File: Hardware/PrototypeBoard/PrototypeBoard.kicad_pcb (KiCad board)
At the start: 2 copper layers, 135 parts, among them J1 Motor, J2 Encoder, J3 ControlSupplyConnector, Q1 Q_NMOS_SGD, Q2 Q_NMOS_SGD, Q3 Q_NMOS_SGD, Q4 Q_NMOS_SGD, Q5 Q_NMOS_SGD, Q6 Q_NMOS_SGD, U1 TLI4970-D025T4, U2 TLI4970-D025T4, U3 TLI4970-D025T4, U4 TLE7185-1E, U5 ADC124S021

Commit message: some more layout work
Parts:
- moved TP31 227.2 mm to (262.9, 138.4)
- moved TP32 220.9 mm to (262.9, 143.5)
- moved TP33 209.2 mm to (260.4, 135.9)
- moved TP34 203.0 mm to (260.4, 141.0)
- moved TP3 194.6 mm to (234.9, 106.7)
- moved TP4 192.0 mm to (234.9, 116.8)
- moved TP5 190.1 mm to (234.9, 127.0)
- moved TP1 183.3 mm to (174.0, 156.2)
- moved TP21 177.9 mm to (209.6, 127.0)
- moved TP2 172.5 mm to (174.0, 148.6)
- moved TP16 162.4 mm to (196.8, 105.4)
- moved TP13 161.8 mm to (209.6, 101.6)
- moved R6 161.7 mm to (265.4, 125.7)
- moved TP14 158.3 mm to (209.6, 111.8)
- moved TP17 156.6 mm to (196.8, 110.5)
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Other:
- board outline added: 152.4 x 101.6 mm

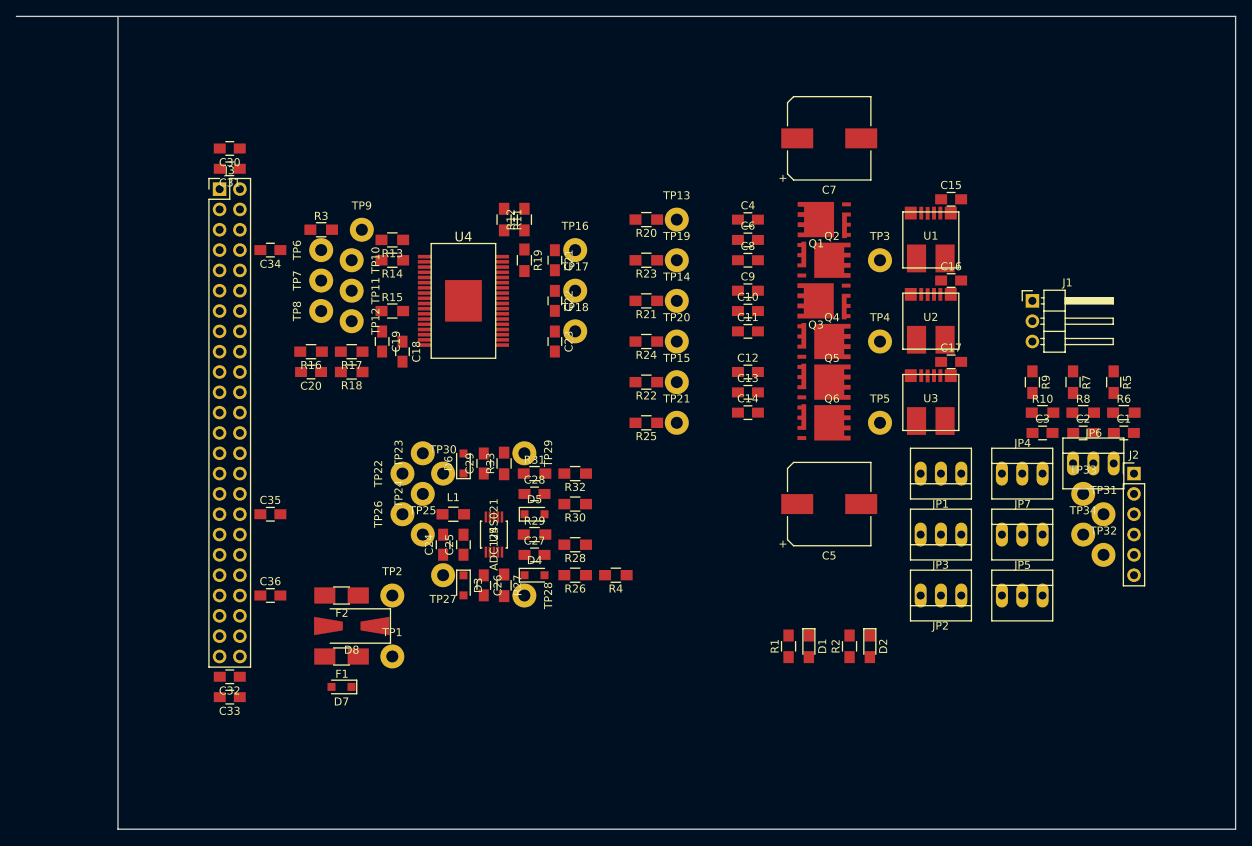
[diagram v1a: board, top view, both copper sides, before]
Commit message: assigned net classes and a few net names
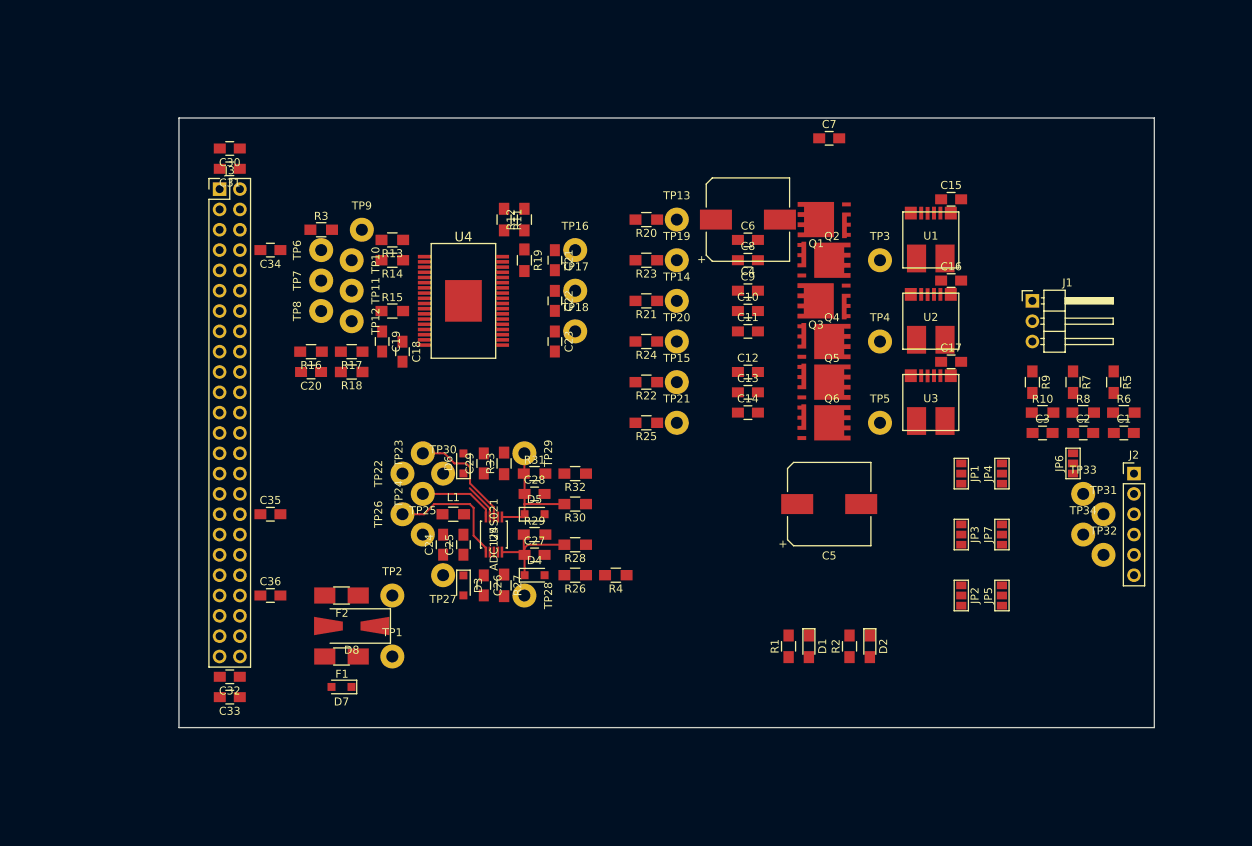
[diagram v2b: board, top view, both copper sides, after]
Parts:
- C4: value 100n -> 220μF, 50V; footprint Capacitors_SMD:C_0805_HandSoldering -> Capacitors_SMD:CP_Elec_10x10
- C6: value 4.7μ, 50V -> 100n
- C7: value 220μF, 50V -> 4.7μ, 50V; footprint Capacitors_SMD:CP_Elec_10x10 -> Capacitors_SMD:C_0805_HandSoldering
- JP1, JP2, JP3, JP4, JP5, JP6, JP7: footprint Connectors:PINHEAD1-3 -> Connectors:GS3
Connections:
- net Net-(C30-Pad1) renamed /MainConnector/PowerIn
- net Net-(C34-Pad2) renamed /MainConnector/3V3in
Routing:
- net /MainConnector/~AdcSpiCs: track 0.00 -> 15.8 mm
- net Net-(C28-Pad1): track 0.00 -> 15.6 mm
- net Net-(C27-Pad1): track 0.00 -> 14.1 mm
- net /MainConnector/AdcSpiMosi: track 0.00 -> 14.1 mm
- net /MainConnector/AdcSpiSclk: track 0.00 -> 9.63 mm
- net /MainConnector/AdcSpiMiso: track 0.00 -> 4.64 mm
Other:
- board size 152.4 x 101.6 mm -> 121.9 x 76.2 mm
- net class High Power Supply added: clearance 0.2, trace_width 1, via_dia 0.6, via_drill 0.4
- net class Low Power Supply added: clearance 0.2, trace_width 0.5, via_dia 0.6, via_drill 0.4

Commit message: minor progress in layout
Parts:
- TP1, TP10, TP11, TP12, TP13, TP14, TP15, TP16, TP17, TP18, TP19, TP2, TP20, TP21, TP22, TP23, TP24, TP25, TP26, TP27, TP28, TP29, TP3, TP30, TP31, TP32, TP33, TP34, TP4, TP5, TP6, TP7, TP8, TP9: footprint Measurement_Points:Measurement_Point_Round-TH_Big -> Measurement_Points:Measurement_Point_Round-SMD-Pad_Small
- moved C4 12.7 mm to (228.6, 94.0)
- moved C7 8.98 mm to (219.7, 92.7)
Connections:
- net Net-(R20-Pad2) renamed /MotorModule/GateDriver/Gate_U_H_bR
- net Net-(R21-Pad2) renamed /MotorModule/GateDriver/Gate_V_H_bR
- net Net-(R22-Pad2) renamed /MotorModule/GateDriver/Gate_W_H_bR
- net Net-(R23-Pad2) renamed /MotorModule/GateDriver/Gate_U_L_bR
- net Net-(R24-Pad2) renamed /MotorModule/GateDriver/Gate_V_L_bR
- net Net-(R25-Pad2) renamed /MotorModule/GateDriver/Gate_W_L_bR
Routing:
- net Net-(C28-Pad1): track 15.6 -> 0.00 mm
- net Net-(C27-Pad1): track 14.1 -> 0.00 mm
- net /MainConnector/AdcSpiMiso: track 4.64 -> 13.7 mm
- net Net-(C24-Pad2): track 0.00 -> 6.07 mm
- net Net-(C29-Pad1): track 0.00 -> 2.55 mm

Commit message: some more layout...
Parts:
- removed the C17 at (243.8, 119.4)
- added C15: 100n, Capacitors_SMD:C_0805_HandSoldering, F.Cu at (244.5, 95.2)
- added C18: 1μ, Capacitors_SMD:C_0805_HandSoldering, F.Cu at (244.5, 106.4)
- added C19: 100n, Capacitors_SMD:C_0805_HandSoldering, F.Cu at (244.5, 120.7)
- added C20: 1μ, Capacitors_SMD:C_0805_HandSoldering, F.Cu at (244.5, 119.1)
- added R26: 0, Resistors_SMD:R_0805_HandSoldering, F.Cu at (176.5, 144.1)
- C16: value 100n -> 1μ
- moved C1 28.6 mm to (294.0, 129.5), turned to 90 degrees
- moved R5 27.1 mm to (290.2, 129.5)
- moved R6 26.9 mm to (292.1, 129.5), turned to 90 degrees
- moved C2 26.1 mm to (286.4, 129.5), turned to 90 degrees
- moved R7 24.7 mm to (282.6, 129.5)
- moved R8 24.4 mm to (284.5, 129.5), turned to 90 degrees
- moved C3 23.5 mm to (278.8, 129.5), turned to 90 degrees
- moved R9 22.3 mm to (275.0, 129.5)
- moved R10 21.9 mm to (276.9, 129.5), turned to 90 degrees
- moved C16 15.5 mm to (244.5, 93.7)
- moved JP2 13.1 mm to (256.5, 142.2)
- moved JP4 12.5 mm to (261.6, 138.4)
- moved JP5 12.5 mm to (261.6, 143.5)
- moved JP1 12.0 mm to (256.5, 137.2)
- moved JP3 8.98 mm to (254.0, 139.7)
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- renumbered C15 to C17, C18 to C21, C19 to C22, C20 to C23, C21 to C24, C22 to C25, C23 to C26, C24 to C27, C25 to C28, C26 to C29, C27 to C30, C28 to C31, C29 to C32, C30 to C33, C31 to C34, C32 to C35, C33 to C36, C34 to C37, C35 to C38, C36 to C39, R26 to R27, R27 to R28, R28 to R29, R29 to R30, R30 to R31, R31 to R32, R32 to R33, R33 to R34
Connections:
- L1 pad 1: +3V3 -> Net-(L1-Pad1)
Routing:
- net /MotorModule/Adc/ADC_IN2: track 0.00 -> 20.5 mm
- net Net-(C1-Pad1): track 0.00 -> 20.3 mm
- net /MotorModule/Adc/ADC_IN3: track 0.00 -> 17.1 mm
- net +3V3: track 0.00 -> 10.7 mm
- net Net-(J2-Pad4): track 0.00 -> 7.62 mm
- net Net-(J2-Pad2): track 0.00 -> 7.62 mm
- net /MotorModule/EncoderConnector/HALL_C: track 0.00 -> 5.61 mm
- net /MotorModule/EncoderConnector/HALL_A: track 0.00 -> 5.61 mm
- net /MotorModule/EncoderConnector/HALL_B: track 0.00 -> 5.61 mm
- net Net-(J2-Pad5): track 0.00 -> 5.08 mm
- net Net-(J2-Pad3): track 0.00 -> 5.08 mm
- added copper zone on F.Cu, net +BATT
- added copper zone on F.Cu, net /MotorModule/CurrentSensing/Power_Phase_U
- added copper zone on F.Cu, net /MotorModule/CurrentSensing/Power_Phase_U_measured
- added copper zone on F.Cu, net /MotorModule/CurrentSensing/Power_Phase_V
- added copper zone on F.Cu, net /MotorModule/CurrentSensing/Power_Phase_V_measured
- added copper zone on F.Cu, net /MotorModule/CurrentSensing/Power_Phase_W
- added copper zone on F.Cu, net /MotorModule/CurrentSensing/Power_Phase_W_measured

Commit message: more layout and some changes to schematic
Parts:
- added C40: 100n, Capacitors_SMD:C_0805_HandSoldering, F.Cu at (241.0, 90.0)
- C33, C36: value 4.7μ -> 100n
- C34, C37: value 100n -> 4.7μ
- J1: value Motor -> Conn_01x03; footprint Pin_Headers:Pin_Header_Angled_1x03_Pitch2.54mm -> Connectors_Phoenix:PhoenixContact_MSTBA-G_03x5.08mm_Angled
- J2: value Encoder -> Conn_01x06; footprint Pin_Headers:Pin_Header_Straight_1x06_Pitch2.54mm -> Pin_Headers:Pin_Header_Straight_1x06_Pitch2.00mm
- J3: footprint Pin_Headers:Pin_Header_Straight_2x24_Pitch2.54mm -> Pin_Headers:Pin_Header_Straight_2x24_Pitch2.00mm
- TP1, TP10, TP11, TP12, TP13, TP14, TP15, TP16, TP17, TP18, TP19, TP2, TP20, TP21, TP22, TP23, TP24, TP25, TP26, TP27, TP28, TP29, TP3, TP30, TP4, TP5, TP6, TP7, TP8, TP9: footprint Measurement_Points:Measurement_Point_Round-SMD-Pad_Small -> Pin_Headers:Pin_Header_Straight_1x01_Pitch2.00mm
- TP31: value EncSclk/HallA -> !EncCs/HallB; footprint Measurement_Points:Measurement_Point_Round-SMD-Pad_Small -> Pin_Headers:Pin_Header_Straight_1x01_Pitch2.00mm
- TP32: value !EncCs/HallB -> EncMiso/HallC; footprint Measurement_Points:Measurement_Point_Round-SMD-Pad_Small -> Pin_Headers:Pin_Header_Straight_1x01_Pitch2.00mm
- TP33: value EncMosi/NC -> EncSclk/HallA; footprint Measurement_Points:Measurement_Point_Round-SMD-Pad_Small -> Pin_Headers:Pin_Header_Straight_1x01_Pitch2.00mm
- TP34: value EncMiso/HallC -> EncMosi/NC; footprint Measurement_Points:Measurement_Point_Round-SMD-Pad_Small -> Pin_Headers:Pin_Header_Straight_1x01_Pitch2.00mm
- moved TP21 148.1 mm to (76.5, 64.5)
- moved R25 146.5 mm to (76.5, 60.5), turned to 90 degrees
- moved TP15 140.8 mm to (81.5, 66.0)
- moved TP13 139.6 mm to (81.5, 43.5)
- moved R22 139.1 mm to (81.5, 62.0), turned to 90 degrees
- moved TP12 138.7 mm to (44.0, 54.0)
- moved TP20 138.4 mm to (84.0, 58.5)
- moved TP5 137.9 mm to (112.0, 67.0)
- moved TP11 137.9 mm to (44.0, 52.0)
- moved R24 137.9 mm to (81.5, 57.0), turned to 90 degrees
- moved TP4 137.6 mm to (112.0, 55.0)
- moved TP3 137.3 mm to (112.0, 43.0)
- moved TP10 137.2 mm to (44.0, 50.0)
- moved R21 136.5 mm to (82.5, 53.0)
- moved C16 136.4 mm to (120.0, 38.0)
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- renumbered JP5 to JP4, JP7 to JP5, JP4 to JP6, JP6 to JP7
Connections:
- C33 pad 1: /MainConnector/PowerIn -> +3V3
- C33 pad 2: GNDPWR -> GND
- C37 pad 1: GND -> /MainConnector/PowerIn
- C37 pad 2: /MainConnector/3V3in -> GNDPWR
- C38 pad 1: /MainConnector/3V3in -> GND
- C38 pad 2: GND -> /MainConnector/3V3in
- J1 pad 1: /MotorModule/CurrentSensing/Power_Phase_U_measured -> /MotorModule/CurrentSensing/Power_Phase_W_measured
- J1 pad 3: /MotorModule/CurrentSensing/Power_Phase_W_measured -> /MotorModule/CurrentSensing/Power_Phase_U_measured
- J3 pad 10: /MainConnector/~PwmUH -> /MainConnector/~GateDriverErr1
- J3 pad 11: /MainConnector/PwmVL -> GND
- J3 pad 12: /MainConnector/~PwmVH -> /MainConnector/GateDriverEna
- J3 pad 13: /MainConnector/PwmWL -> /MainConnector/PwmUL
- J3 pad 14: /MainConnector/~PwmWH -> /MainConnector/~PwmUH
- J3 pad 15: /MainConnector/~GateDriverErr1 -> /MainConnector/PwmVL
- J3 pad 16: /MainConnector/~GateDriverErr2 -> /MainConnector/~PwmVH
- J3 pad 17: GND -> /MainConnector/PwmWL
- J3 pad 18: /MainConnector/GateDriverEna -> /MainConnector/~PwmWH
- J3 pad 9: /MainConnector/PwmUL -> /MainConnector/~GateDriverErr2
- JP4 pad 1: /MotorModule/EncoderConnector/HALL_B -> GND
- JP4 pad 3: /MainConnector/~EncoderSpiCs -> /MainConnector/EncoderSpiMiso
- JP5 pad 3: /MainConnector/EncoderSpiMiso -> /MainConnector/EncoderSpiMosi
- JP6 pad 1: /MotorModule/EncoderConnector/HALL_A -> /MotorModule/EncoderConnector/HALL_B
- JP6 pad 3: /MainConnector/EncoderSpiSclk -> /MainConnector/~EncoderSpiCs
- JP7 pad 1: /MainConnector/EncoderSpiMosi -> /MotorModule/EncoderConnector/HALL_A
- JP7 pad 3: GND -> /MainConnector/EncoderSpiSclk
- TP31 pad 1: Net-(J2-Pad3) -> Net-(J2-Pad5)
- TP32 pad 1: Net-(J2-Pad5) -> Net-(J2-Pad4)
- TP33 pad 1: Net-(J2-Pad2) -> Net-(J2-Pad3)
- TP34 pad 1: Net-(J2-Pad4) -> Net-(J2-Pad2)
- U1 pad 6: /MotorModule/CurrentSensing/Logic_OCD -> /MotorModule/GateDriver/Logic_GD_ENA
- U2 pad 6: /MotorModule/CurrentSensing/Logic_OCD -> /MotorModule/GateDriver/Logic_GD_ENA
- U3 pad 6: /MotorModule/CurrentSensing/Logic_OCD -> /MotorModule/GateDriver/Logic_GD_ENA
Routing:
- net (no net): track 0.00 -> 43.1 mm, vias 0 -> 3
- net Net-(C1-Pad1): track 20.3 -> 0.00 mm
- net /MotorModule/Adc/ADC_IN2: track 20.5 -> 5.93 mm
- net /MainConnector/EncoderSpiSclk: track 0.00 -> 13.7 mm
- net /MainConnector/~GateDriverErr2: track 0.00 -> 13.1 mm
- net /MotorModule/Adc/ADC_IN3: track 17.1 -> 5.93 mm
- net /MainConnector/~GateDriverErr1: track 0.00 -> 11.1 mm
- net /MainConnector/~PwmVH: track 0.00 -> 9.00 mm
- net /MotorModule/GateDriver/Gate_U_L_bR: track 0.00 -> 8.65 mm
- net /MotorModule/GateDriver/Gate_V_H_bR: track 0.00 -> 8.42 mm
- net Net-(C24-Pad1): track 0.00 -> 7.78 mm
- net GND: track 0.00 -> 7.30 mm
- net /MotorModule/CurrentSensing/Power_Phase_U: track 0.00 -> 6.75 mm
- net /MotorModule/CurrentSensing/Power_Phase_V: track 0.00 -> 6.25 mm
- net Net-(C27-Pad2): track 6.07 -> 0.00 mm
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- added copper zone on B.Cu, net +BATT
- added copper zone on B.Cu, net GND
- added copper zone on F.Cu, net GND
- added copper zone on F.Cu, net GNDPWR
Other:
- board size 121.9 x 76.2 mm -> 100 x 60 mm
- copper layers 2 -> 4

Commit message: More Layout...
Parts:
- added D8: 30V, Diodes_SMD:D_SMA-SMB_Universal_Handsoldering, F.Cu at (41.0, 86.0)
- moved F2 175.4 mm to (41.0, 33.0)
- moved D7 159.8 mm to (43.0, 75.0)
- moved F1 158.0 mm to (42.0, 78.5)
- moved D9 147.3 mm to (48.0, 97.0)
- moved C40 117.0 mm to (124.0, 88.0)
- moved J2 117.0 mm to (128.0, 78.0)
- moved TP31 117.0 mm to (126.0, 86.0)
- moved TP32 117.0 mm to (126.0, 84.0)
- moved TP33 117.0 mm to (126.0, 82.0)
- moved TP34 117.0 mm to (126.0, 80.0)
- moved JP1 117.0 mm to (118.5, 78.5)
- moved JP2 117.0 mm to (118.5, 81.0)
- moved JP3 117.0 mm to (118.5, 83.5)
- moved JP4 117.0 mm to (122.5, 86.0)
- moved JP5 117.0 mm to (122.5, 83.5)
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- renumbered D8 to D9
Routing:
- net /MainConnector/CurrentSensSpiSclk: track 0.00 -> 79.5 mm, vias 0 -> 3
- net /MainConnector/~CurrentSensSpiCs: track 0.00 -> 75.4 mm, vias 0 -> 3
- net /MainConnector/CurrentSensSpiDoutU: track 0.00 -> 72.1 mm, vias 0 -> 1
- net /MainConnector/CurrentSensSpiDoutV: track 0.00 -> 57.0 mm, vias 0 -> 1
- net /MainConnector/CurrentSensSpiDoutW: track 0.00 -> 41.9 mm, vias 0 -> 1
- net /MainConnector/~EncoderSpiCs: track 2.76 -> 43.4 mm, vias 1 -> 2
- net /MainConnector/EncoderSpiMosi: track 3.85 -> 43.1 mm, vias 1 -> 2
- net /MainConnector/EncoderSpiMiso: track 4.85 -> 42.5 mm, vias 1 -> 2
- net /MainConnector/EncoderSpiSclk: track 13.7 -> 44.5 mm
- net /MotorModule/CurrentSensing/Power_Phase_U_measured: track 0.00 -> 22.1 mm
- net /MotorModule/Adc/ADC_IN2: track 5.93 -> 25.3 mm
- net /MotorModule/CurrentSensing/Power_Phase_V_measured: track 0.00 -> 18.0 mm
- net /MotorModule/Adc/ADC_IN3: track 5.93 -> 21.3 mm
- net (no net): track 43.1 -> 31.1 mm, vias 3 -> 0
- net +BATT: track 0.00 -> 5.91 mm, vias 0 -> 1
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- added copper zone on In1.Cu, net +3V3
- added copper zone on F.Cu, net /MainConnector/3V3in
- added copper zone on In1.Cu, net /MainConnector/3V3in
- added copper zone on B.Cu, net /MainConnector/PowerIn
- added copper zone on F.Cu, net /MainConnector/PowerIn
- added copper zone on In1.Cu, net /MainConnector/PowerIn
- added copper zone on In2.Cu, net GND
- added copper zone on B.Cu, net GNDPWR

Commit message: layout and some pin swapping...
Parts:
- moved TP15 2.24 mm to (77.5, 64.0)
- moved TP16 2.24 mm to (71.0, 49.0)
- moved TP20 1.50 mm to (77.5, 58.5)
- moved TP13 1.12 mm to (75.5, 44.0)
- moved C24 1.00 mm to (73.0, 48.0)
- moved C25 1.00 mm to (73.0, 53.0)
- moved C26 1.00 mm to (73.0, 58.0)
- moved R20 1.00 mm to (75.5, 47.0)
- moved R22 1.00 mm to (75.5, 62.0)
- moved R24 1.00 mm to (75.5, 57.0)
- moved TP14 1.00 mm to (80.5, 53.0)
- moved TP17 1.00 mm to (71.0, 52.0)
- moved TP19 1.00 mm to (80.5, 50.5)
- moved R25 0.71 mm to (71.0, 61.0)
- moved TP21 0.71 mm to (71.0, 64.0)
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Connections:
- J3 pad 21: GND -> /MainConnector/~CurrentSensSpiCs
- J3 pad 22: /MainConnector/CurrentSensSpiDoutU -> /MainConnector/CurrentSensSpiDoutW
- J3 pad 23: /MainConnector/~CurrentSensSpiCs -> GND
- J3 pad 26: /MainConnector/CurrentSensSpiDoutW -> /MainConnector/CurrentSensSpiDoutU
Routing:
- net /MotorModule/CurrentSensing/Power_Phase_W: track 0.00 -> 18.4 mm
- net /MainConnector/CurrentSensSpiDoutU: track 72.1 -> 86.1 mm, vias 1 -> 2
- net /MainConnector/CurrentSensSpiDoutV: track 57.0 -> 70.2 mm, vias 1 -> 2
- net /MainConnector/CurrentSensSpiDoutW: track 41.9 -> 54.3 mm, vias 1 -> 2
- net /MotorModule/GateDriver/Gate_W_L: track 0.00 -> 12.3 mm
- net /MainConnector/CurrentSensSpiSclk: track 79.5 -> 91.2 mm, vias 3 -> 4
- net /MainConnector/~CurrentSensSpiCs: track 75.4 -> 86.3 mm, vias 3 -> 4
- net /MotorModule/GateDriver/Gate_U_L_bR: track 8.65 -> 0.00 mm
- net /MotorModule/GateDriver/Gate_V_H_bR: track 8.42 -> 0.00 mm
- net Net-(C24-Pad1): track 7.78 -> 0.00 mm
- net /MotorModule/CurrentSensing/Power_Phase_U: track 6.75 -> 0.00 mm
- net /MotorModule/CurrentSensing/Power_Phase_V: track 6.25 -> 0.00 mm
- net Net-(C26-Pad1): track 0.00 -> 5.48 mm
- net /MotorModule/GateDriver/Gate_W_L_bR: track 0.00 -> 3.87 mm
- net Net-(C25-Pad1): track 2.10 -> 0.00 mm

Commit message: more Layout...
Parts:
- moved C32 126.5 mm to (62.0, 70.5)
- moved TP28 126.5 mm to (72.0, 83.5)
- moved D6 126.5 mm to (60.0, 70.8)
- moved C27 126.5 mm to (59.0, 80.0)
- moved C28 126.5 mm to (61.0, 80.0)
- moved C29 126.5 mm to (62.0, 85.0)
- moved C30 126.5 mm to (68.0, 82.0)
- moved C31 126.5 mm to (68.0, 76.0)
- moved D3 126.5 mm to (60.0, 85.0)
- moved D4 126.5 mm to (68.0, 84.0)
- moved R26 126.5 mm to (57.0, 80.0)
- moved R27 126.5 mm to (68.0, 86.0)
- moved R28 126.5 mm to (64.0, 85.0)
- moved R29 126.5 mm to (72.0, 80.0)
- moved R30 126.5 mm to (68.0, 80.0)
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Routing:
- net (no net): track 31.1 -> 15.4 mm
- net /MotorModule/CurrentSensing/Power_Phase_U: track 0.00 -> 14.2 mm
- net Net-(C25-Pad1): track 0.00 -> 14.0 mm
- net /MotorModule/CurrentSensing/Power_Phase_V: track 0.00 -> 13.7 mm
- net /MotorModule/GateDriver/Gate_W_H_bR: track 0.10 -> 9.83 mm
- net /MotorModule/GateDriver/Gate_U_H_bR: track 0.00 -> 9.41 mm
- net /MotorModule/GateDriver/Gate_U_L_bR: track 0.00 -> 8.15 mm
- net /MotorModule/GateDriver/Gate_V_L_bR: track 0.00 -> 8.06 mm
- net /MotorModule/GateDriver/Gate_V_H_bR: track 0.00 -> 7.92 mm
- net Net-(C24-Pad1): track 0.00 -> 6.78 mm
- net Net-(R11-Pad2): track 2.00 -> 5.18 mm
- net /MotorModule/GateDriver/Gate_W_H: track 0.00 -> 2.27 mm
- net /MotorModule/GateDriver/Gate_U_H: track 0.00 -> 2.15 mm
- net /MotorModule/GateDriver/Gate_V_L: track 0.00 -> 2.06 mm
- net /MainConnector/AdcSpiSclk: track 7.63 -> 6.91 mm
